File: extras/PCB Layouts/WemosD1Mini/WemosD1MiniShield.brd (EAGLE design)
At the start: 25.4 x 27.4 mm, 13 parts, among them T1 BC817-40, U2 WEMOS-D1-MINI-SHIELD

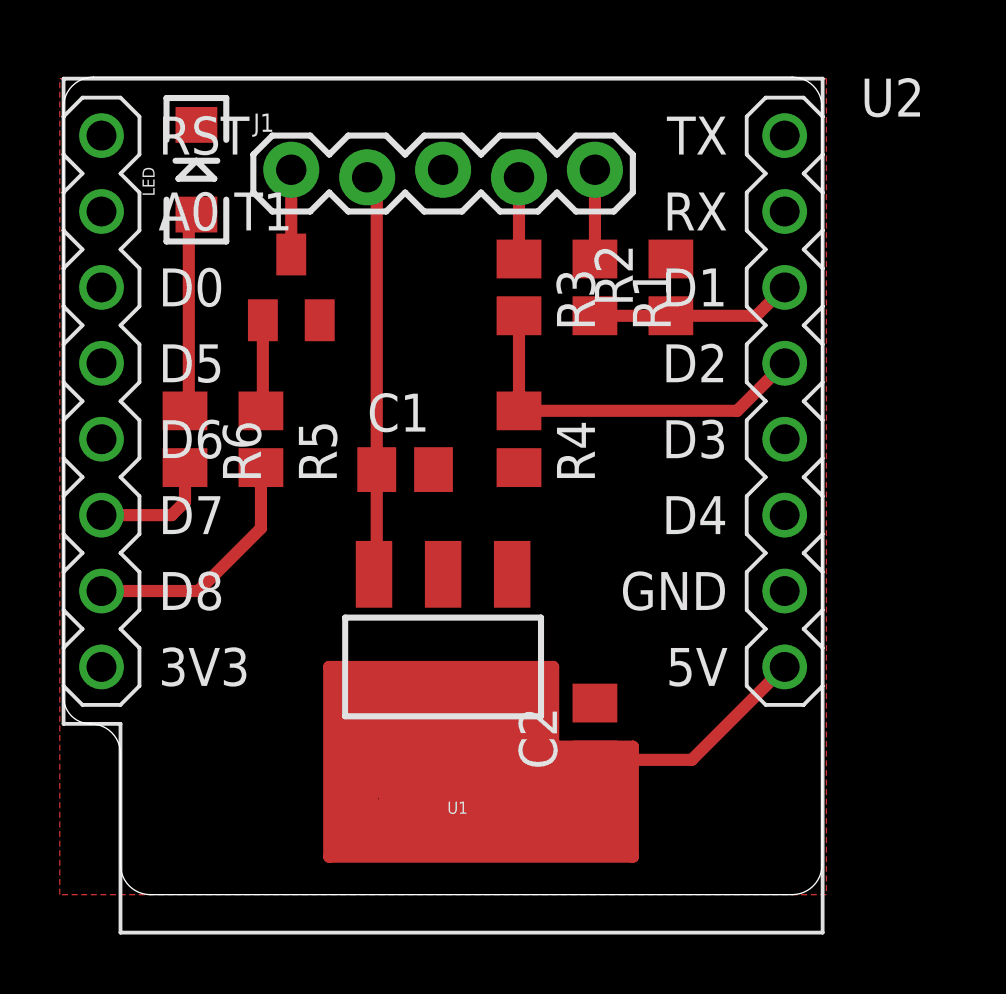
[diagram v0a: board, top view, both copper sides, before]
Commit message: Changed components to bottom layer for easier DIY.
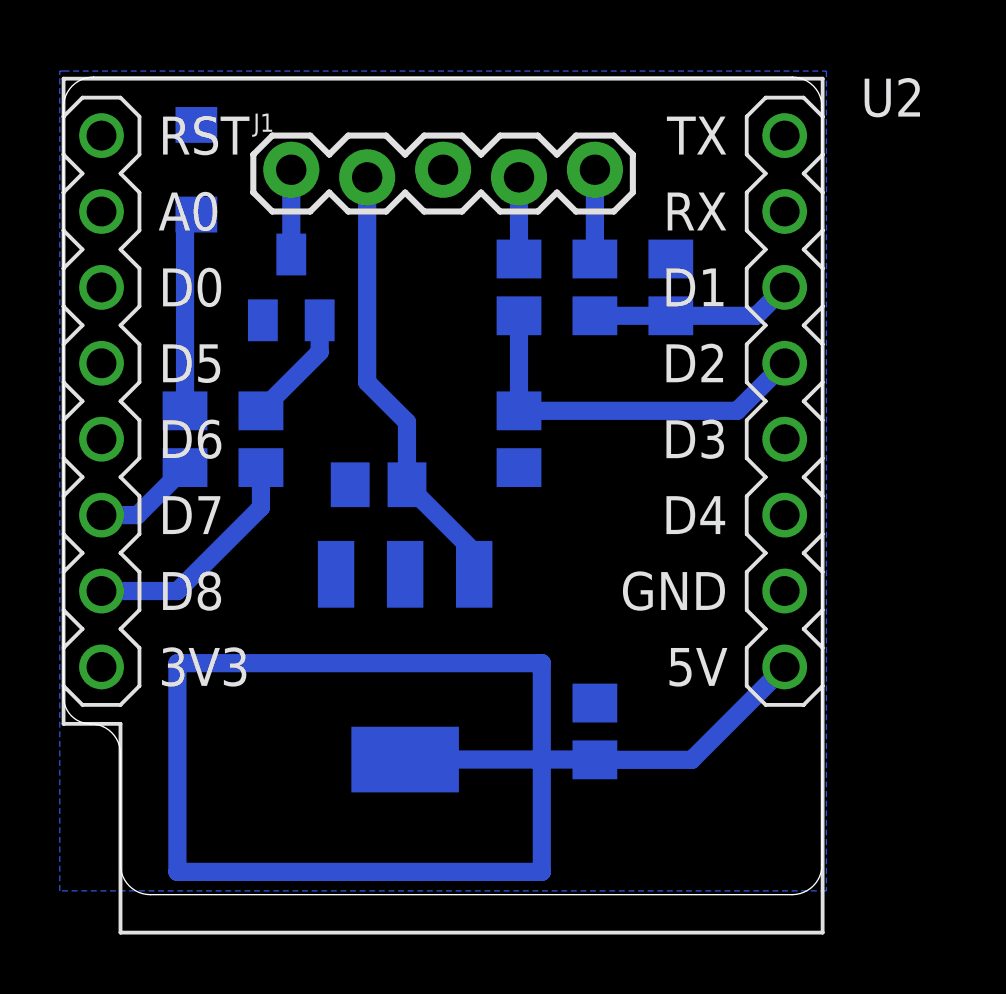
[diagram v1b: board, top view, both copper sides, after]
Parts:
- moved U1 1.27 mm to (11.4, 8.89), flipped to the bottom
- moved C1 1.02 mm to (10.5, 15.0), flipped to the bottom
- flipped C2 to the bottom
- flipped LED to the bottom
- flipped R1 to the bottom
- flipped R2 to the bottom
- flipped R3 to the bottom
- flipped R4 to the bottom
- flipped R5 to the bottom
- flipped R6 to the bottom
- flipped T1 to the bottom
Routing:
- net +5V: track 169.4 -> 52.4 mm
- net +12V: track 13.5 -> 14.8 mm
- net N$4: track 3.51 -> 4.39 mm
- net D7_LED: track 4.12 -> 3.45 mm
- net N$5: track 6.72 -> 7.26 mm
- added copper zone on layer 16, net +5V
- added copper zone on layer 16, net GND
- removed copper zone on layer 1, net GND
